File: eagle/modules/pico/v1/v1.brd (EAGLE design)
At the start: 85.7 x 50.8 mm, 36 parts, among them IC1 MEGA8-AI, IC3 ULN2803A, IC4 ULN2803A, J1 RJ12STRAIGHT-RS232-SERVER

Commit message: Update pico
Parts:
- added C3: 10uF 20V, SparkFun:EIA3216-KIT
- added C4: 100 nF, SparkFun:1206
- added D1: 1N581D1206, lpatiny:LED-1206
- added LED4: (no value), lpatiny:LED3MM
- added Q1: FDN340P, lpatiny:SUPER-SOT3
- added RL4: 1K, resistor:M1206
- moved CON1 78.2 mm to (85.1, 24.8), turned to 90 degrees
- moved R1 14.8 mm to (88.9, 6.35), turned to 270 degrees
- moved R7 7.41 mm to (85.1, 6.35), turned to 270 degrees
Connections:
- new net 5V: C1.1, C2.1, C3.A, C4.1, D1.C, IC1.18, IC1.4, IC1.6, Q1.2, R1.2, R7.2, R8.2, RL4.1, U$1.3
- new net ISP+5V: CON1.VCC, D1.A, Q1.1
- new net N$7: LED4.A, RL4.2
- net +5V: now also Q1.3; no longer C1.1, C2.1, CON1.VCC, IC1.18, IC1.4, IC1.6, R1.2, R7.2, R8.2, U$1.3
- net GND: now also C3.C, C4.2, LED4.K
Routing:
- net GND: track 297.1 -> 312.3 mm
- net +12V: track 219.4 -> 234.7 mm
- net +5V: track 218.9 -> 231.1 mm
- net N$6: track 18.5 -> 16.7 mm
- net SCK: track 0.64 -> 0.00 mm
- net RESET: track 0.64 -> 0.00 mm
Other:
- board size 85.7 x 50.8 mm -> 93.3 x 53.3 mm

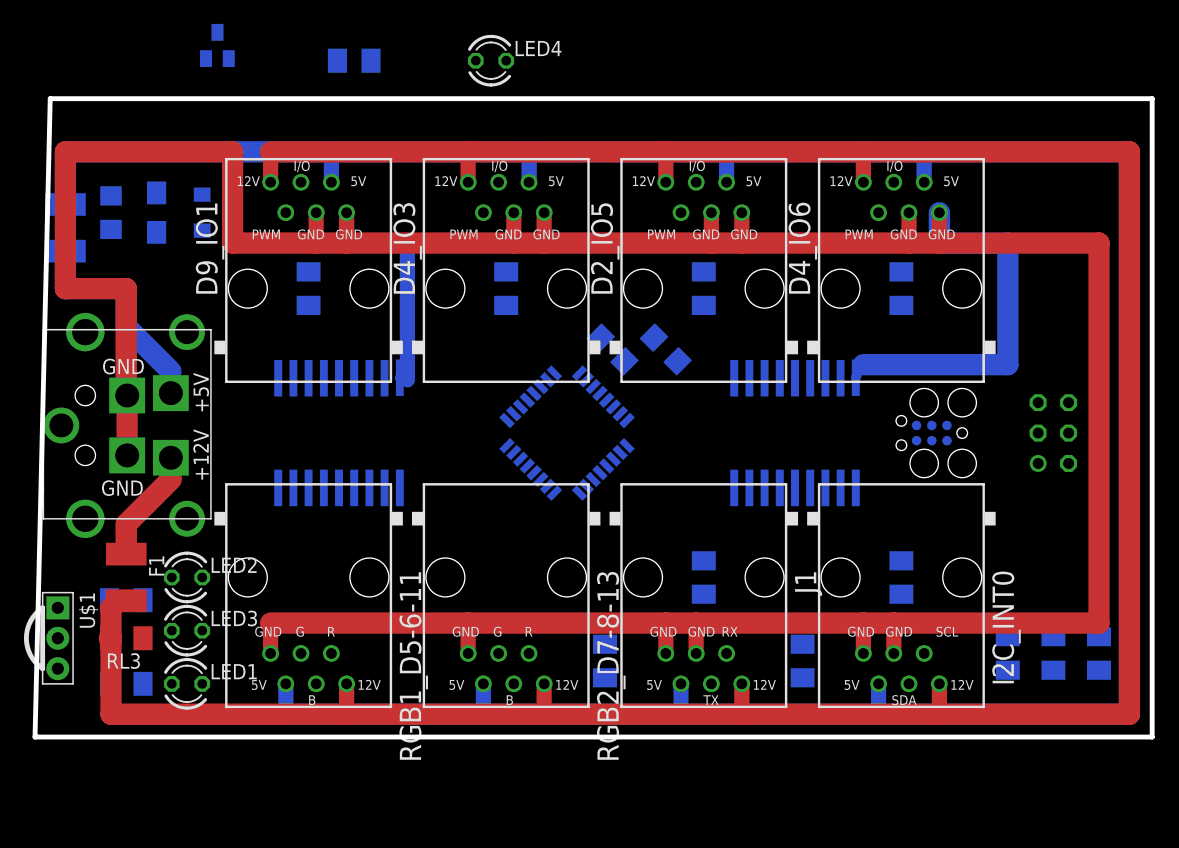
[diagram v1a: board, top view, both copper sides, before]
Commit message: Update board size
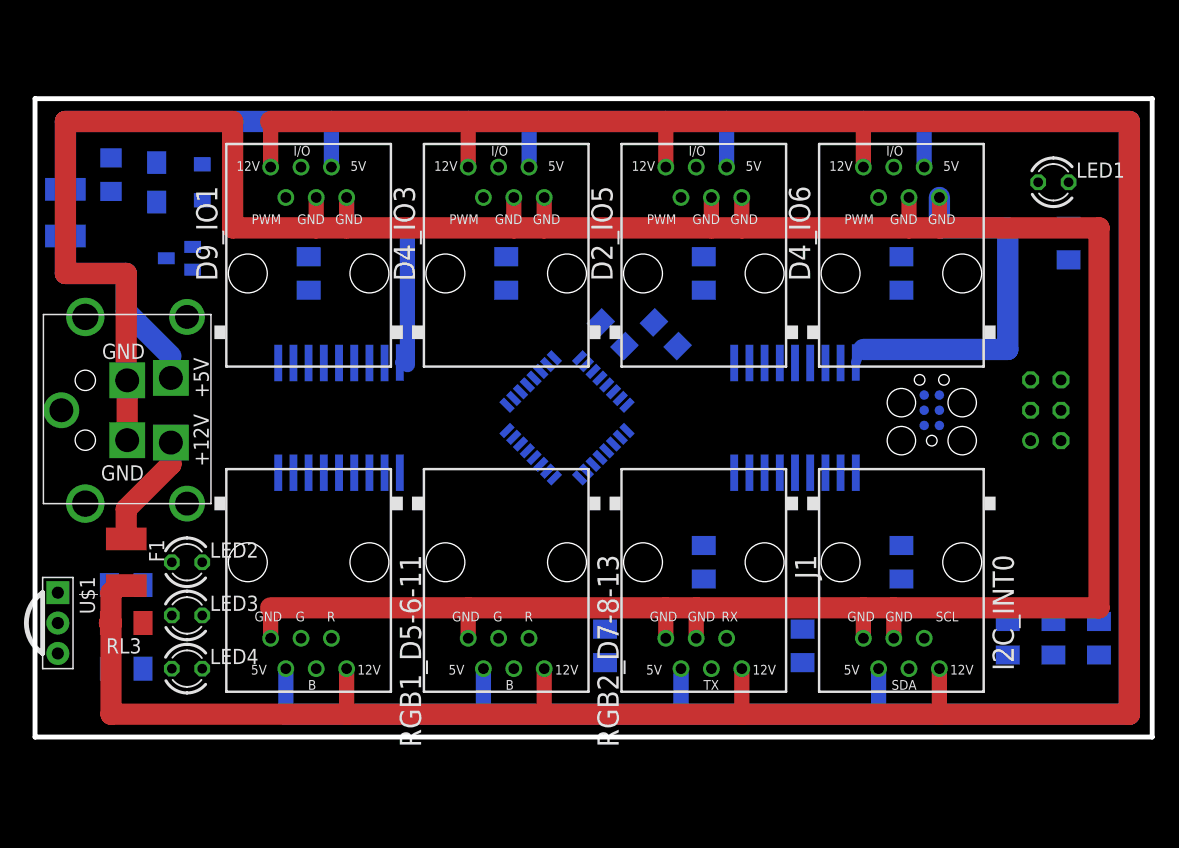
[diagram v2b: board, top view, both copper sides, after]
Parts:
- moved RL1 86.9 mm to (86.4, 40.6), turned to 270 degrees
- moved LED1 83.6 mm to (85.1, 45.7)
- moved LED4 56.8 mm to (12.7, 5.08)
- moved RL4 54.3 mm to (7.62, 5.08), turned to 180 degrees
- moved Q1 18.1 mm to (12.1, 39.4), turned to 270 degrees
- moved C4 3.17 mm to (6.35, 46.4)
- moved J2 2.62 mm to (74.9, 24.1), turned to 90 degrees
- moved C3 2.54 mm to (10.2, 45.7)
- moved D1 2.54 mm to (14.0, 45.7)
- moved CON1 2.01 mm to (84.5, 26.7)
- moved C1 1.27 mm to (48.3, 33.0)
- moved C2 1.27 mm to (52.7, 33.0)
- moved D2_IO5 1.27 mm to (55.9, 38.1)
- moved D4_IO3 1.27 mm to (39.4, 38.1)
- moved D4_IO6 1.27 mm to (72.4, 38.1)
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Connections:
- removed net D13: LED1.A
- net SCK: now also LED1.A
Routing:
- net +12V: track 234.7 -> 248.6 mm
- net +5V: track 231.1 -> 245.1 mm
- net GND: track 312.3 -> 314.9 mm
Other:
- outline, holes or cut-outs redrawn

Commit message: Remove transistor
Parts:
- removed C4: 100 nF, SparkFun:1206
- removed Q1: FDN340P, lpatiny:SUPER-SOT3
- added D2: 1N581D1206, lpatiny:LED-1206
- moved C3 2.54 mm to (7.62, 45.7)
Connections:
- net +5V: now also D2.A; no longer Q1.3
- net 5V: now also D2.C; no longer C4.1, Q1.2
- net GND: no longer C4.2
- net ISP+5V: no longer Q1.1
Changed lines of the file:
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@@
 <element name="F2" library="lpatiny" package="C1812" value="POLYSWITCHSMD1812" x="2.54" y="43.18" rot="MR90"/>
 <element name="F1" library="lpatiny" package="C1812" value="POLYSWITCHSMD1812" x="7.62" y="13.97" rot="R270"/>
-<element name="C3" library="SparkFun" package="EIA3216-KIT" value="10uF 20V" x="10.16" y="45.72" rot="MR90"/>
-<element name="C4" library="SparkFun" package="1206" value="100 nF" x="6.35" y="46.355" rot="MR270"/>
+<element name="C3" library="SparkFun" package="EIA3216-KIT" value="10uF 20V" x="7.62" y="45.72" rot="MR90"/>
 <element name="D1" library="lpatiny" package="LED-1206" value="1N581D1206" x="13.97" y="45.72" rot="MR90"/>
 <element name="LED4" library="lpatiny" package="LED3MM" value="" x="12.7" y="5.08"/>
 <element name="RL4" library="resistor" package="M1206" value="1K" x="7.62" y="5.08" rot="MR180"/>
-<element name="Q1" library="lpatiny" package="SUPER-SOT3" value="FDN340P" x="12.065" y="39.37" rot="MR270">
-<attribute name="FND340P" value="" x="12.065" y="39.37" size="1.778" layer="28" rot="MR270" display="off"/>
-<attribute name="FND360P" value="" x="12.065" y="39.37" size="1.778" layer="28" rot="MR270" display="off"/>
-</element>
+<element name="D2" library="lpatiny" package="LED-1206" value="1N581D1206" x="11.43" y="40.64" rot="MR0"/>
 </elements>
 <signals>
@@
 <contactref element="RL1" pad="2"/>
 <contactref element="C3" pad="C"/>
-<contactref element="C4" pad="2"/>
 <contactref element="LED4" pad="K"/>
 <wire x1="88.9" y1="41.91" x2="86.36" y2="39.24" width="0" layer="19" extent="1-16"/>
 <wire x1="26.035" y1="41.91" x2="26.035" y2="41.91" width="0" layer="19" extent="1-16"/>
-<wire x1="6.35" y1="44.955" x2="7.62" y2="38.1" width="0" layer="19" extent="1-16"/>
-<wire x1="10.16" y1="44.07" x2="6.35" y2="44.955" width="0" layer="19" extent="16-16"/>
+<wire x1="85.725" y1="29.21" x2="81.28" y2="31.75" width="0" layer="19" extent="16-16"/>
 <wire x1="13.97" y1="9.525" x2="19.685" y2="10.16" width="0" layer="19" extent="1-1"/>
 <wire x1="13.97" y1="13.97" x2="13.97" y2="9.525" width="0" layer="19" extent="1-1"/>
 <wire x1="13.97" y1="5.08" x2="13.97" y2="9.525" width="0" layer="19" extent="1-1"/>
-<wire x1="85.725" y1="29.21" x2="81.28" y2="31.75" width="0" layer="19" extent="16-16"/>
+<wire x1="7.62" y1="44.07" x2="7.62" y2="38.1" width="0" layer="19" extent="1-16"/>
 <wire x1="53.69495" y1="32.03005" x2="56.515" y2="41.91" width="0" layer="19" extent="1-16"/>
 <wire x1="47.768171875" y1="28.78748125" x2="53.69495" y2="32.03005" width="0" layer="19" extent="16-16"/>
-<wire x1="42.263203125" y1="22.15114375" x2="47.768171875" y2="28.78748125" width="0" layer="19" extent="16-16"/>
-<wire x1="41.13183125" y1="23.282515625" x2="42.263203125" y2="22.15114375" width="0" layer="19" extent="16-16"/>
+<wire x1="41.13183125" y1="23.282515625" x2="47.768171875" y2="28.78748125" width="0" layer="19" extent="16-16"/>
+<wire x1="42.263203125" y1="22.15114375" x2="41.13183125" y2="23.282515625" width="0" layer="19" extent="16-16"/>
 <wire x1="1.905" y1="8.89" x2="13.97" y2="9.525" width="0" layer="19" extent="1-1"/>
 </signal>
@@
 <contactref element="D1" pad="C"/>
 <contactref element="C3" pad="A"/>
-<contactref element="C4" pad="1"/>
 <contactref element="R7" pad="2"/>
 <contactref element="R8" pad="2"/>
 <contactref element="U$1" pad="3"/>
 <contactref element="RL4" pad="1"/>
-<contactref element="Q1" pad="2"/>
+<contactref element="D2" pad="C"/>
 <wire x1="85.09" y1="6.22" x2="88.9" y2="6.22" width="0" layer="19" extent="16-16"/>
 <wire x1="64.135" y1="5.585" x2="85.09" y2="6.22" width="0" layer="19" extent="16-16"/>
@@
 <wire x1="47.270053125" y1="34.009946875" x2="46.071115625" y2="30.4845375" width="0" layer="19" extent="16-16"/>
 <wire x1="51.715053125" y1="34.009946875" x2="47.270053125" y2="34.009946875" width="0" layer="19" extent="16-16"/>
-<wire x1="13.165" y1="38.42" x2="40.566146875" y2="23.8482" width="0" layer="19" extent="16-16"/>
-<wire x1="13.97" y1="47.22" x2="13.165" y2="38.42" width="0" layer="19" extent="16-16"/>
-<wire x1="10.16" y1="47.37" x2="13.97" y2="47.22" width="0" layer="19" extent="16-16"/>
-<wire x1="6.35" y1="47.755" x2="10.16" y2="47.37" width="0" layer="19" extent="16-16"/>
-<wire x1="6.22" y1="5.08" x2="13.165" y2="38.42" width="0" layer="19" extent="16-16"/>
+<wire x1="13.97" y1="47.22" x2="40.566146875" y2="23.8482" width="0" layer="19" extent="16-16"/>
+<wire x1="7.62" y1="47.37" x2="13.97" y2="47.22" width="0" layer="19" extent="16-16"/>
+<wire x1="6.22" y1="5.08" x2="40.566146875" y2="23.8482" width="0" layer="19" extent="16-16"/>
 <wire x1="1.905" y1="6.35" x2="6.22" y2="5.08" width="0" layer="19" extent="16-16"/>
+<wire x1="9.93" y1="40.64" x2="6.22" y2="5.08" width="0" layer="19" extent="1-16"/>
 </signal>
 <signal name="N$7">
@@
 </signal>
 <signal name="+5V">
-<contactref element="Q1" pad="3"/>
 <contactref element="RL2" pad="2"/>
 <contactref element="D4_IO3" pad="+5V"/>
@@
 <contactref element="F2" pad="2"/>
 <wire x1="2.54" y1="45.13" x2="2.54" y2="50.8" width="1.778" layer="16"/>
-<wire x1="6.22" y1="12.065" x2="10.965" y2="39.37" width="0" layer="19" extent="16-16"/>
-<wire x1="20.955" y1="5.08" x2="6.22" y2="12.065" width="0" layer="19" extent="16-16"/>
+<contactref element="D2" pad="A"/>
+<wire x1="6.22" y1="12.065" x2="20.955" y2="5.08" width="0" layer="19" extent="16-16"/>
+<wire x1="12.93" y1="40.64" x2="6.22" y2="12.065" width="0" layer="19" extent="1-16"/>
 </signal>
 <signal name="ISP+5V">
 <contactref element="CON1" pad="VCC"/>
 <contactref element="D1" pad="A"/>
-<contactref element="Q1" pad="1"/>
-<wire x1="13.165" y1="40.32" x2="85.725" y2="24.13" width="0" layer="19" extent="16-16"/>
-<wire x1="13.97" y1="44.22" x2="13.165" y2="40.32" width="0" layer="19" extent="16-16"/>
+<wire x1="13.97" y1="44.22" x2="85.725" y2="24.13" width="0" layer="19" extent="16-16"/>
 </signal>
 </signals>
